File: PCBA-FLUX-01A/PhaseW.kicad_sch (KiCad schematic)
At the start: 60 parts, among them Q12 IPT015N10N5, Q13 IPT015N10N5, Q14 IPT015N10N5, Q15 IPT015N10N5, Q16 BC817, U10 TLV9001, U8 INA240A2DR, U9 UCC27211AQDDARQ1

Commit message: Changes were made
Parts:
- added C106: C, Capacitor_THT:C_Rect_L9.0mm_W6.4mm_P7.50mm_MKT, symbol Device:C
- added C97: 10nF, Capacitor_SMD:C_0603_1608Metric, symbol Device:C
- added R84, R85, R86, R87: 10R, Resistor_SMD:R_0805_2012Metric, symbol Device:R
- added R92: R, Resistor_SMD:R_1218_3246Metric, symbol Device:R
- R51, R52, R53, R67: footprint Resistor_SMD:R_0805_2012Metric -> Resistor_SMD:R_0603_1608Metric
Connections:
- net GND: now also C106.2
- net phW_Shunt+: now also R84.1, R85.1; no longer U8.8 (IN+)
- net phW_Shunt-: now also R86.1, R87.1; no longer U8.1 (IN-)
- net at C81.2, C82.2, Q12.2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: now also R92.1
- new net: C97.2, R86.2, R87.2, U8.1 (IN-)
- new net: C97.1, R84.2, R85.2, U8.8 (IN+)
- new net: C106.1, R92.2
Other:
- moved on the sheet: C75, C76, C77, C78, C79, C80, C81, C82, D10, D11, D12, D13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

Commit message: Finished schematic?
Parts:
- removed C83: 3.3nF, Capacitor_SMD:C_0603_1608Metric, symbol Device:C
- removed C84, C92: 100nF, Capacitor_SMD:C_0402_1005Metric, symbol Device:C
- removed C85: 1nF, Capacitor_SMD:C_0603_1608Metric, symbol Device:C
- removed C86, C88, C90, C93: 2.2uF, Capacitor_SMD:C_1210_3225Metric, symbol Device:C
- removed C87, C89, C91, C94: 100nF, Capacitor_SMD:C_0805_2012Metric, symbol Device:C
- removed Q14, Q15: IPT015N10N5, Package_TO_SOT_SMD:Infineon_PG-HSOF-8-1_ThermalVias, symbol Bvrny's_library:IPT015N10N5
- removed Q16: BC817, Package_TO_SOT_SMD:SOT-23, symbol Transistor_BJT:BC817
- removed R68: 10k, Resistor_SMD:R_1206_3216Metric, symbol Device:R
- removed R70: 0.1mR, Bvrny's_library:R5930, symbol Device:R_Shunt
- removed R73: 0R, Resistor_SMD:R_0603_1608Metric, symbol Device:R
- removed R74: 2K2, Resistor_SMD:R_0603_1608Metric, symbol Device:R
- removed R75: 10K, Resistor_SMD:R_0603_1608Metric, symbol Device:R
- removed U8: INA240A2DR, Package_SO:SOIC-8_3.9x4.9mm_P1.27mm, symbol Bvrny's_library:INA240A2DR
- removed U9: UCC27211AQDDARQ1, Package_SO:SOIC-8-1EP_3.9x4.9mm_P1.27mm_EP2.95x4.9mm_Mask2.34x2.34mm_ThermalVias, symbol Bvrny's_library:UCC27211AQDDARQ1
- added C129, C131, C133, C135, C137: 1000uF, Capacitor_THT:CP_Radial_D18.0mm_P7.50mm, symbol Device:C_Polarized
- added C130, C132, C134, C136, C138: 10uF, Capacitor_SMD:C_1210_3225Metric, symbol Device:C
- added C139: 100nF, Capacitor_SMD:C_0805_2012Metric, symbol Device:C
- added C65, C67: 22uF, Capacitor_SMD:C_1206_3216Metric, symbol Device:C
- added C66, C68, C71: 100nF, Capacitor_SMD:C_0402_1005Metric, symbol Device:C
- added C69, C70: 1nF, Capacitor_SMD:C_0603_1608Metric, symbol Device:C
- added C72: 2.2uF, Capacitor_SMD:C_1206_3216Metric, symbol Device:C
- added Q10, Q11: IPT015N10N5, Package_TO_SOT_SMD:Infineon_PG-HSOF-8-1_ThermalVias, symbol Bvrny's_library:IPT015N10N5
- added Q20: BC860C, Package_TO_SOT_SMD:SOT-23, symbol Simulation_SPICE:PNP
- added R49, R50: 100R, Resistor_SMD:R_0603_1608Metric, symbol Device:R
- added R68: 0.1mR, Bvrny's_library:R5930, symbol Device:R_Shunt
- added R70: 560R, Resistor_SMD:R_0603_1608Metric, symbol Device:R
- added R95: 18k, Resistor_SMD:R_0603_1608Metric, symbol Synapse:R
- added U8: UCC27211AQDDARQ1, Package_SO:SOIC-8-1EP_3.9x4.9mm_P1.27mm_EP2.95x4.9mm_Mask2.34x2.34mm_ThermalVias, symbol Bvrny's_library:UCC27211AQDDARQ1
- added U9: INA240A2DR, Package_SO:SOIC-8_3.9x4.9mm_P1.27mm, symbol Bvrny's_library:INA240A2DR
- C73: value 100nF -> 2.2nF; footprint Capacitor_SMD:C_0402_1005Metric -> Capacitor_SMD:C_0603_1608Metric; JLCPCB Part # C307331 -> C1604; JLCPCB price https://jlcpcb.com/partdetail/291005-CL05B104KB54PNC/C307331 -> https://jlcpcb.com/partdetail/1956-0603B222K500NT/C1604; MFR.Part # CL05B104KB54PNC -> 0603B222K500NT; Manufacturer Samsung Electro-Mechanics -> FH (Guangdong Fenghua Advanced Tech); Package 0402 -> 0603
- C75: value 22uF -> 3.3nF; footprint Capacitor_SMD:C_1206_3216Metric -> Capacitor_SMD:C_0603_1608Metric; Dielectric X5R -> X7R; JLCPCB Part # C12891 -> C1613; JLCPCB price https://jlcpcb.com/partdetail/13537-CL31A226KAHNNNE/C12891 -> https://jlcpcb.com/partdetail/1965-CL10B332KB8NNNC/C1613; MFR.Part # CL31A226KAHNNNE -> CL10B332KB8NNNC; Manufacturer Samsung Electro-Mechanics -> Samsung Electro-Mechanics; Package 1206 -> 0603; Voltage 25V -> 50V
- C76: value 22uF -> 100nF; footprint Capacitor_SMD:C_1206_3216Metric -> Capacitor_SMD:C_0402_1005Metric; Dielectric X5R -> X7R; JLCPCB Part # C12891 -> C307331; JLCPCB price https://jlcpcb.com/partdetail/13537-CL31A226KAHNNNE/C12891 -> https://jlcpcb.com/partdetail/291005-CL05B104KB54PNC/C307331; MFR.Part # CL31A226KAHNNNE -> CL05B104KB54PNC; Package 1206 -> 0402; Voltage 25V -> 50V
- C78: value 1nF -> 100nF; footprint Capacitor_SMD:C_0603_1608Metric -> Capacitor_SMD:C_0805_2012Metric; JLCPCB Part # C1588 -> C28233; JLCPCB price https://jlcpcb.com/partdetail/1940-CL10B102KB8NNNC/C1588 -> https://jlcpcb.com/partdetail/28983-CL21B104KCFNNNE/C28233; MFR.Part # CL10B102KB8NNNC -> CL21B104KCFNNNE; Package 0603 -> 0805; Voltage 50V -> 100V
- C79, C82: footprint Capacitor_SMD:C_0402_1005Metric -> Capacitor_SMD:C_0805_2012Metric; JLCPCB Part # C307331 -> C28233; JLCPCB price https://jlcpcb.com/partdetail/291005-CL05B104KB54PNC/C307331 -> https://jlcpcb.com/partdetail/28983-CL21B104KCFNNNE/C28233; MFR.Part # CL05B104KB54PNC -> CL21B104KCFNNNE; Package 0402 -> 0805; Voltage 50V -> 100V
- C80: value 2.2nF -> 100nF; footprint Capacitor_SMD:C_0603_1608Metric -> Capacitor_SMD:C_0805_2012Metric; JLCPCB Part # C1604 -> C28233; JLCPCB price https://jlcpcb.com/partdetail/1956-0603B222K500NT/C1604 -> https://jlcpcb.com/partdetail/28983-CL21B104KCFNNNE/C28233; MFR.Part # 0603B222K500NT -> CL21B104KCFNNNE; Manufacturer FH (Guangdong Fenghua Advanced Tech) -> Samsung Electro-Mechanics; Package 0603 -> 0805; Voltage 50V -> 100V
- C81: value 2.2uF -> 100nF; footprint Capacitor_SMD:C_1206_3216Metric -> Capacitor_SMD:C_0402_1005Metric; JLCPCB Part # C50254 -> C307331; JLCPCB price https://jlcpcb.com/partdetail/51263-CL31B225KBHNNNE/C50254 -> https://jlcpcb.com/partdetail/291005-CL05B104KB54PNC/C307331; MFR.Part # CL31B225KBHNNNE -> CL05B104KB54PNC; Package 1206 -> 0402; Voltage 50V -> (none); Voltage rating (none) -> 50V
- R51: footprint Resistor_SMD:R_0603_1608Metric -> palmkiLib:R_0603_1608Metric
- R52, R53: value 100R -> 1R; footprint Resistor_SMD:R_0603_1608Metric -> Resistor_SMD:R_1206_3216Metric; JLCPCB Part # C22775 -> C17928; JLCPCB price https://jlcpcb.com/partdetail/23502-0603WAF1000T5E/C22775 -> https://jlcpcb.com/partdetail/18616-1206W4F100KT5E/C17928; MFR.Part # 0603WAF1000T5E -> 1206W4F100KT5E; Package 0603 -> 1206
- R54, R55, R63, R64: value 1R -> 3R3; JLCPCB Part # C17928 -> C2783335; JLCPCB price https://jlcpcb.com/partdetail/18616-1206W4F100KT5E/C17928 -> https://jlcpcb.com/partdetail/2921791-NS06W4F330KT5E/C27833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; MFR.Part # 1206W4F100KT5E -> NS06W4F330KT5E
- R56, R57, R65, R66: value 3R3 -> 10k; JLCPCB Part # C2783335 -> C17902; JLCPCB price https://jlcpcb.com/partdetail/2921791-NS06W4F330KT5E/C27833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 -> https://jlcpcb.com/partdetail/18590-1206W4F1002T5E/C17902; MFR.Part # NS06W4F330KT5E -> 1206W4F1002T5E
- R58, R59: value 10k -> 51k; footprint Resistor_SMD:R_1206_3216Metric -> Resistor_SMD:R_0805_2012Metric; JLCPCB Part # C17902 -> C17737; JLCPCB price https://jlcpcb.com/partdetail/18590-1206W4F1002T5E/C17902 -> https://jlcpcb.com/partdetail/18425-0805W8F5102T5E/C17737; MFR.Part # 1206W4F1002T5E -> 0805W8F5102T5E; Package 1206 -> 0805
- R60: value 51k -> 4k7; JLCPCB Part # C17737 -> C17673; JLCPCB price https://jlcpcb.com/partdetail/18425-0805W8F5102T5E/C17737 -> https://jlcpcb.com/partdetail/18361-0805W8F4701T5E/C17673; MFR.Part # 0805W8F5102T5E -> 0805W8F4701T5E
- R61: value 51k -> 1R; footprint Resistor_SMD:R_0805_2012Metric -> Resistor_SMD:R_1206_3216Metric; JLCPCB Part # C17737 -> C17928; JLCPCB price https://jlcpcb.com/partdetail/18425-0805W8F5102T5E/C17737 -> https://jlcpcb.com/partdetail/18616-1206W4F100KT5E/C17928; MFR.Part # 0805W8F5102T5E -> 1206W4F100KT5E; Package 0805 -> 1206
- R62: value 4k7 -> 1R; footprint Resistor_SMD:R_0805_2012Metric -> Resistor_SMD:R_1206_3216Metric; JLCPCB Part # C17673 -> C17928; JLCPCB price https://jlcpcb.com/partdetail/18361-0805W8F4701T5E/C17673 -> https://jlcpcb.com/partdetail/18616-1206W4F100KT5E/C17928; MFR.Part # 0805W8F4701T5E -> 1206W4F100KT5E; Package 0805 -> 1206
- R69: value 10k -> 2K2; footprint Resistor_SMD:R_1206_3216Metric -> Resistor_SMD:R_0603_1608Metric; JLCPCB Part # C17902 -> C4190; JLCPCB price https://jlcpcb.com/partdetail/18590-1206W4F1002T5E/C17902 -> https://jlcpcb.com/partdetail/4597-0603WAF2201T5E/C4190; MFR.Part # 1206W4F1002T5E -> 0603WAF2201T5E; Manufacturer UNI-ROYAL(Uniroyal Elec) -> UNI-ROYAL(Uniroyal Elec); Package 1206 -> 0603; Tolerance ±1% -> 1%
- R71: value 2K2 -> 0R; JLCPCB Part # C4190 -> C21189; JLCPCB price https://jlcpcb.com/partdetail/4597-0603WAF2201T5E/C4190 -> https://jlcpcb.com/partdetail/21903-0603WAF0000T5E/C21189; MFR.Part # 0603WAF2201T5E -> 0603WAF0000T5E
- R72: value 560R -> 10K; JLCPCB Part # C23204 -> C25804; JLCPCB price https://jlcpcb.com/partdetail/23931-0603WAF5600T5E/C23204 -> https://jlcpcb.com/partdetail/26547-0603WAF1002T5E/C25804; MFR.Part # 0603WAF5600T5E -> 0603WAF1002T5E
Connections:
- net +12V: now also C65.1, C67.1, C71.1, U8.1 (VDD); no longer C75.1, C76.1, C79.1
- net +3.3VA: now also C76.1, R71.1, C66.1, C68.1, Q20.3 (E), R95.1, U9.3 (REF2), U9.6 (VS); no longer C73.1, C74.1
- net +VSYS: now also C78.1, C79.1, C80.1, C82.1, C129.1, C130.1, C131.1, C132.1, C133.1, C134.1, C135.1, C136.1, C137.1, C138.1, C139.1, Q10.3
- net GND: now also C81.2, C82.2, R57.2, R60.2, R66.2, C129.2, C130.2, C131.2, C132.2, C133.2, C134.2, C135.2, C136.2, C137.2, C138.2, C139.2, C65.2, C66.2, C67.2, C68.2, C69.2, C70.2, C71.2, Q11.2, U8.7 (VSS), U8.9 (Pad), U9.2 (GND), U9.4 (NC), U9.7 (REF1); no longer C74.2, R59.2, R62.2, R69.2
- net HSgate: now also R52.1, R61.1, U8.3 (HO); no longer R56.1, R65.1
- net LSgate: now also R53.1, R62.1, U8.8 (LO); no longer R57.1, R66.1
- net PhaseW_out: now also R58.1, R68.4; no longer R60.1
- net phW_HI: now also R49.1; no longer R51.1
- net phW_LO: now also R50.1; no longer R52.1
- net phW_NTCctrl: now also R69.1; no longer R71.1
- net phW_NTCout: now also C81.1, R72.2
- net phW_current: now also C73.1, R51.2; no longer C80.1, R53.2
- net phW_voltage: now also C77.1
- net at D11.1 (K): now also R53.2; no longer R55.2
- net at R64.2: now also D13.2 (A), Q13.1, R66.1; no longer D13.1 (K)
- net at C97.2, R86.2, R87.2: now also U9.1 (IN-)
- net at TH3.1: now also R72.1, R70.2, R95.2; no longer R72.2
- net at Q12.2, Q13.3, R92.1: now also C74.2, R56.2, R65.2, C72.2, Q10.2, Q11.3, R68.1, U8.4 (HS); no longer C81.2, C82.2, R58.2
- net at C97.1, R84.2, R85.2: now also U9.8 (IN+)
- net at R63.2: now also D12.2 (A), Q12.1, R65.1; no longer D12.1 (K)
- net at R52.2: now also D10.1 (K); no longer C78.1
- net at R54.2: now also D10.2 (A), R56.1, Q10.1; no longer D10.1 (K)
- net at R71.2: now also Q20.1 (C), R70.1
- new net: C72.1, C74.1, U8.2 (HB)
- new net: C69.1, R49.2, U8.5 (HI)
- new net: C70.1, R50.2, U8.6 (LI)
- new net: R58.2, R59.1
- new net: C75.1, R59.2, R60.1, U10.3 (IN+)
- new net: R51.1, U9.5 (OUT)
- new net: Q20.2 (B), R69.2
- new net: D12.1 (K), R61.2
- new net: D11.2 (A), Q11.1, R55.2, R57.1
- new net: D13.1 (K), R62.2
- new net phU_Shunt+: R68.2
- new net phU_Shunt-: R68.3
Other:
- note added: "Current Sense"
- note added: "DC-Link"
- note added: "Gate driver & bridge"
- note added: "Phase Temp"
- note added: "Phase Voltage"

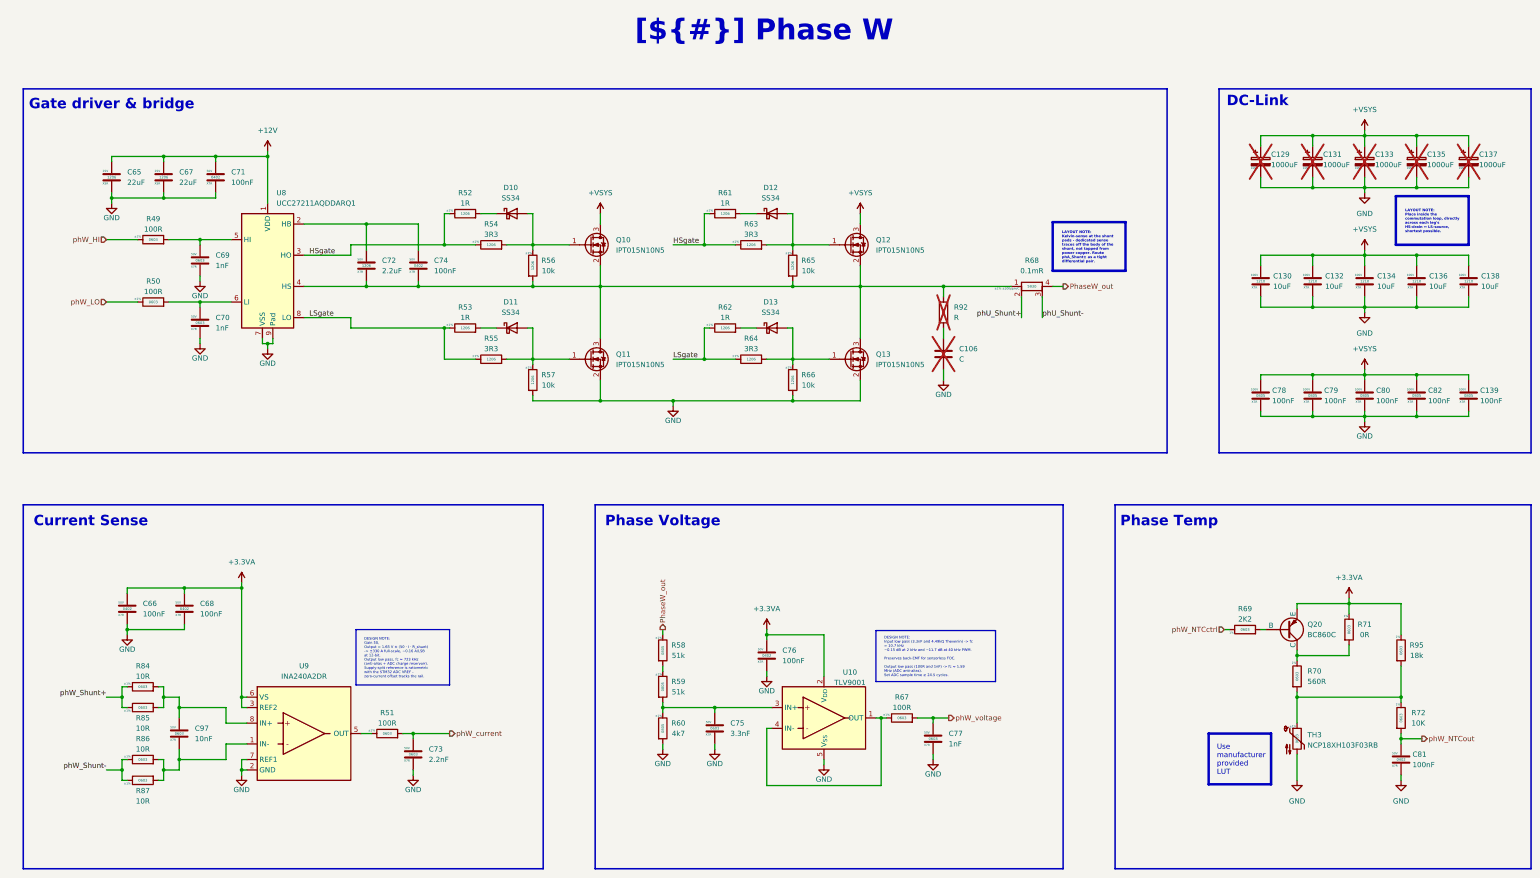
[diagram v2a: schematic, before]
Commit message: Moved the current and voltage sensing OpAmp's to Vector
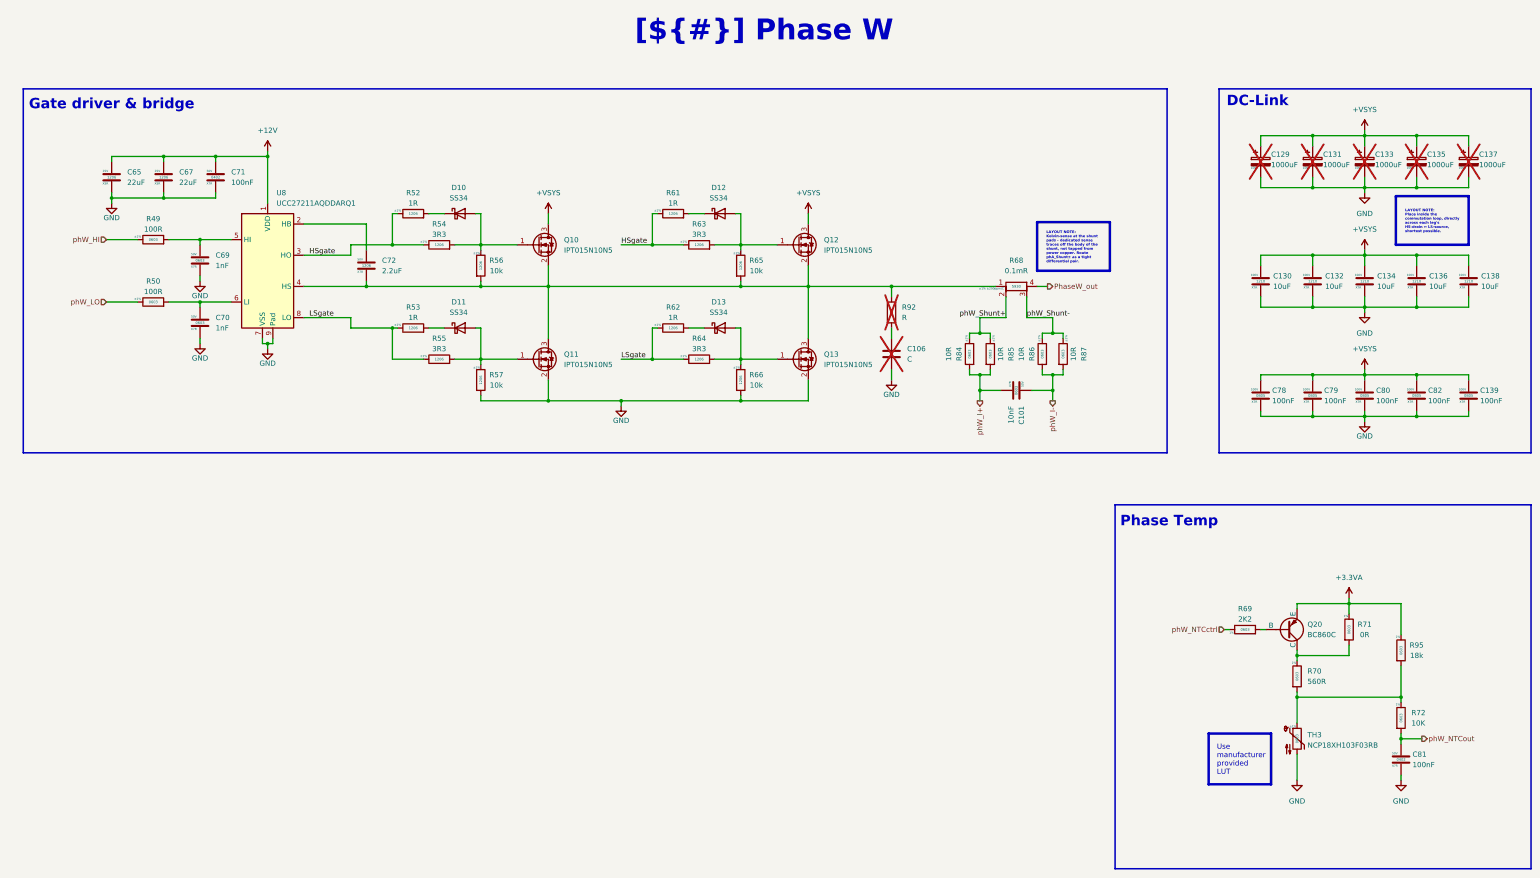
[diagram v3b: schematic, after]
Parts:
- removed C66, C68, C74, C76: 100nF, Capacitor_SMD:C_0402_1005Metric, symbol Device:C
- removed C73: 2.2nF, Capacitor_SMD:C_0603_1608Metric, symbol Device:C
- removed C75: 3.3nF, Capacitor_SMD:C_0603_1608Metric, symbol Device:C
- removed C77: 1nF, Capacitor_SMD:C_0603_1608Metric, symbol Device:C
- removed C97: 10nF, Capacitor_SMD:C_0603_1608Metric, symbol Device:C
- removed R51: 100R, palmkiLib:R_0603_1608Metric, symbol Device:R
- removed R58, R59: 51k, Resistor_SMD:R_0805_2012Metric, symbol Device:R
- removed R60: 4k7, Resistor_SMD:R_0805_2012Metric, symbol Device:R
- removed R67: 100R, Resistor_SMD:R_0603_1608Metric, symbol Device:R
- removed U10: TLV9001, Package_TO_SOT_SMD:SOT-23-5, symbol Bvrny's_library:TLV9001IDBVR
- removed U9: INA240A2DR, Package_SO:SOIC-8_3.9x4.9mm_P1.27mm, symbol Bvrny's_library:INA240A2DR
- added C101: 10nF, Capacitor_SMD:C_0603_1608Metric, symbol Device:C
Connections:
- net phU_Shunt+ is gone; now on net phW_Shunt+: R68.2
- net phU_Shunt- is gone; now on net phW_Shunt-: R68.3
- net phW_I-: now reaches R86.2, R87.2
- net phW_I-: now also C101.1
- net phW_I+: now reaches R84.2, R85.2
- net phW_I+: now also C101.2
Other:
- note removed: "Current Sense"
- note removed: "Phase Voltage"
- moved on the sheet: C106, D10, D11, D12, D13, Q10, Q11, Q12, Q13, R52, R53, R54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
